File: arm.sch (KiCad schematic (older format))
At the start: 83 parts, among them J1 MICROSD_SOCKET_SPI, M1 MOTOR, P1 MicroUSB, P2 HC-05/06, P3 I²C_Port, P4 SPI_Port, P5 Ring_Port, Q1 MOSFET_N, Q2 IRLML2246TRPBF, Q3 IRLML2246TRPBF, Q4 MOSFET_P, Q5 IRLML2246TRPBF, Q6 IRLML2246TRPBF, Q7 IRLML2246TRPBF, Q8 IRLML2246TRPBF, Q9 IRLML2246TRPBF, SW1 SPST, SW2 SPST, U1 STM32F100C8, U2 LTC4054-4.2, U3 LTC2942-1, U4 HMC5883L, U5 MPU6050, U6 LTC3444, U7 BMP085, X1 8 mHz, X2 32.768(MS3V-T1R)

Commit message: Removed invisible labels
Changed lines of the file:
@@
 	1    0    0    -1
 $EndComp
-Text Label 900  4600 2    60   ~ 0
-VCC
-Text Label 900  4400 2    60   ~ 0
-SCL
 Text GLabel 4050 3450 0    60   BiDi ~ 0
 sda

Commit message: 6-pin ring port, RING_BTN2
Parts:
- removed P5: Ring_Port, symbol CONN_5
- added P?: CONN_6, symbol CONN_6
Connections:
- net GND: now also P?.6
- net accelgyro_interrupt: now also U1.39 (PB3/JTDO); no longer U1.45 (PB8/TIM4_CH3/TIM16_CH1/CEC)
- net at Q3.3 (D): now also P?.2
- net at Q5.1 (G), R14.1: now also P?.1
- net at Q6.3 (D): now also P?.3
- net at Q8.3 (D): now also P?.4
- net BT_LED1: no longer names the net of P2.31 (PIO8)
- net BT_LED1: no longer U1.39 (PB3/JTDO)
- net BT_LED2: no longer names the net of U1.40 (PB4/NJRST)
- net BT_LED2: no longer P2.32 (PIO9)
- net RING_BUTTON renamed RING_BTN1
- new net RING_BTN2: P?.5, U1.45 (PB8/TIM4_CH3/TIM16_CH1/CEC)

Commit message: Both PIO0 and PIO11 are connected to BT_KEY now. This is required for HM-10 and HC-05 compatibility.
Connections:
- net BT_KEY: now also P2.23 (PIO0)
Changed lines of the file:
@@
 Wire Wire Line
 	5700 6500 5700 6850
+Entry Wire Line
+	10800 2700 10900 2600
+Wire Wire Line
+	10350 2700 10800 2700
+Text Label 10400 2700 0    60   ~ 0
+BT_KEY
 $EndSCHEMATC

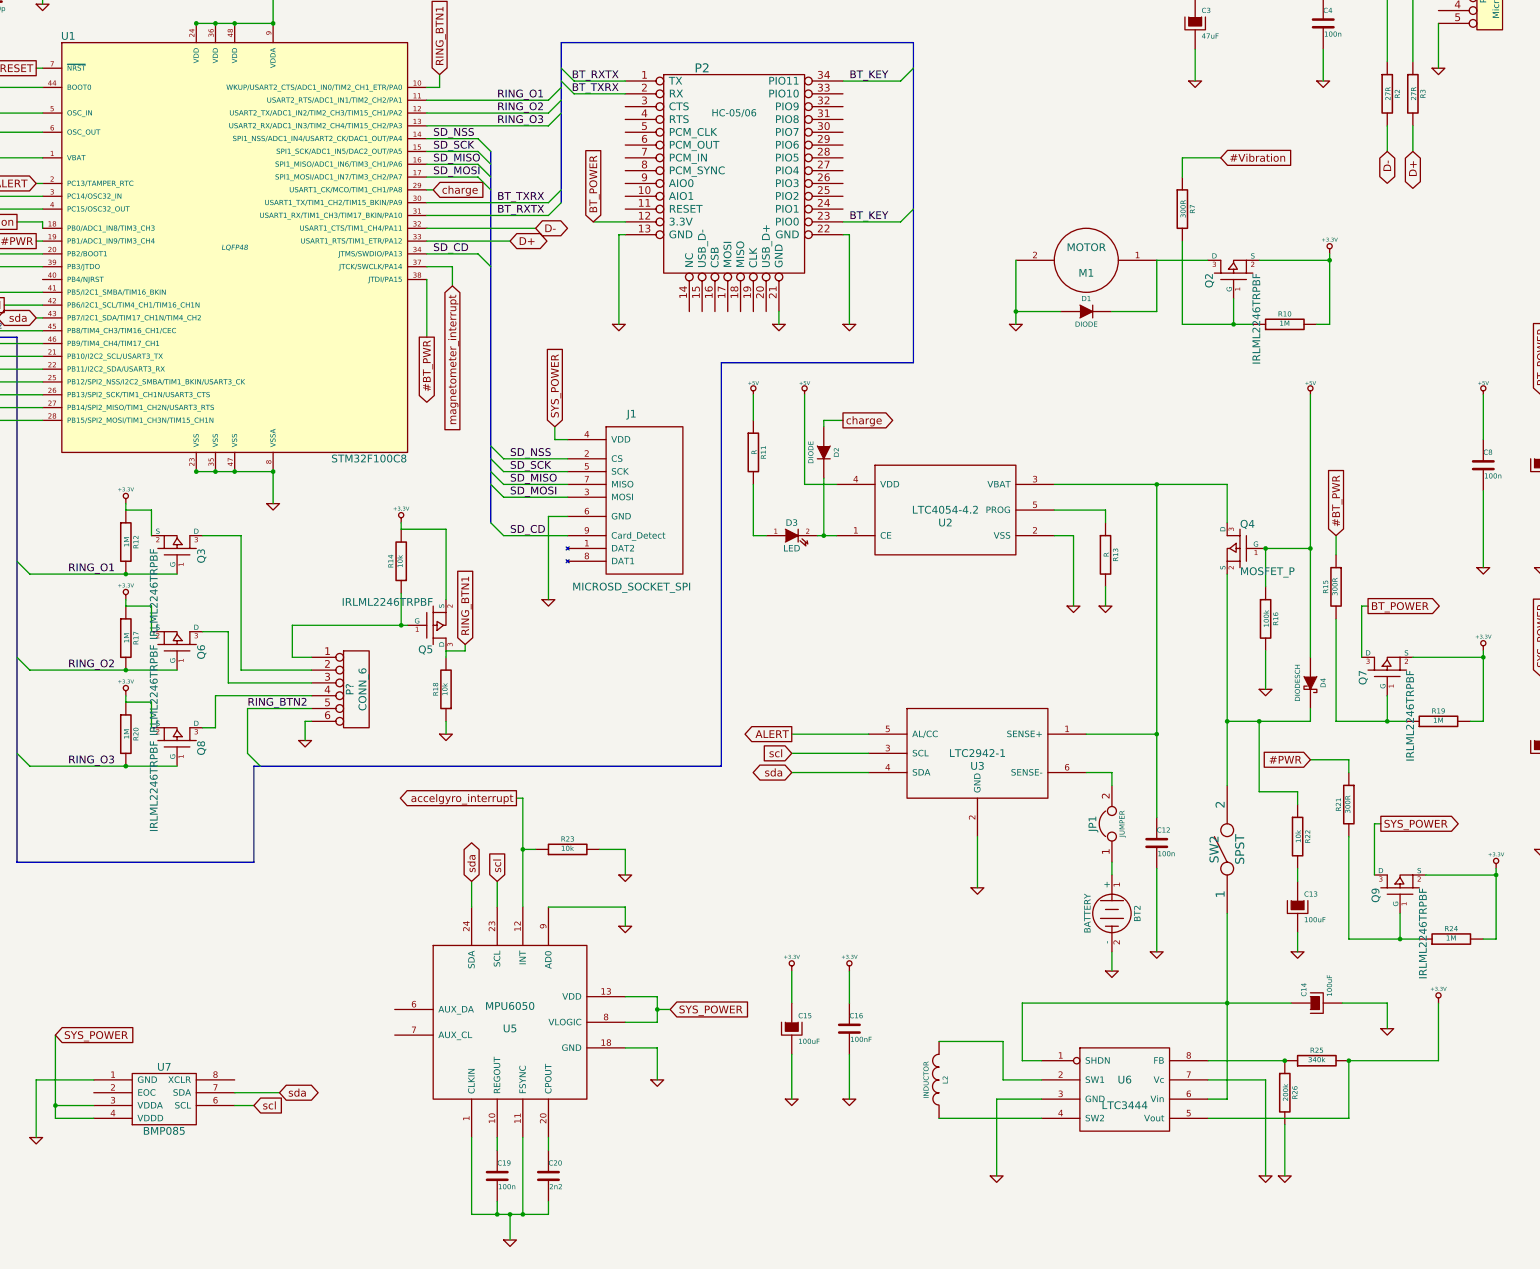
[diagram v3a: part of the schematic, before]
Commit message: Implemented an LTC3566-2 power management IC as primary power source / charge controller instead of previous problematic build.
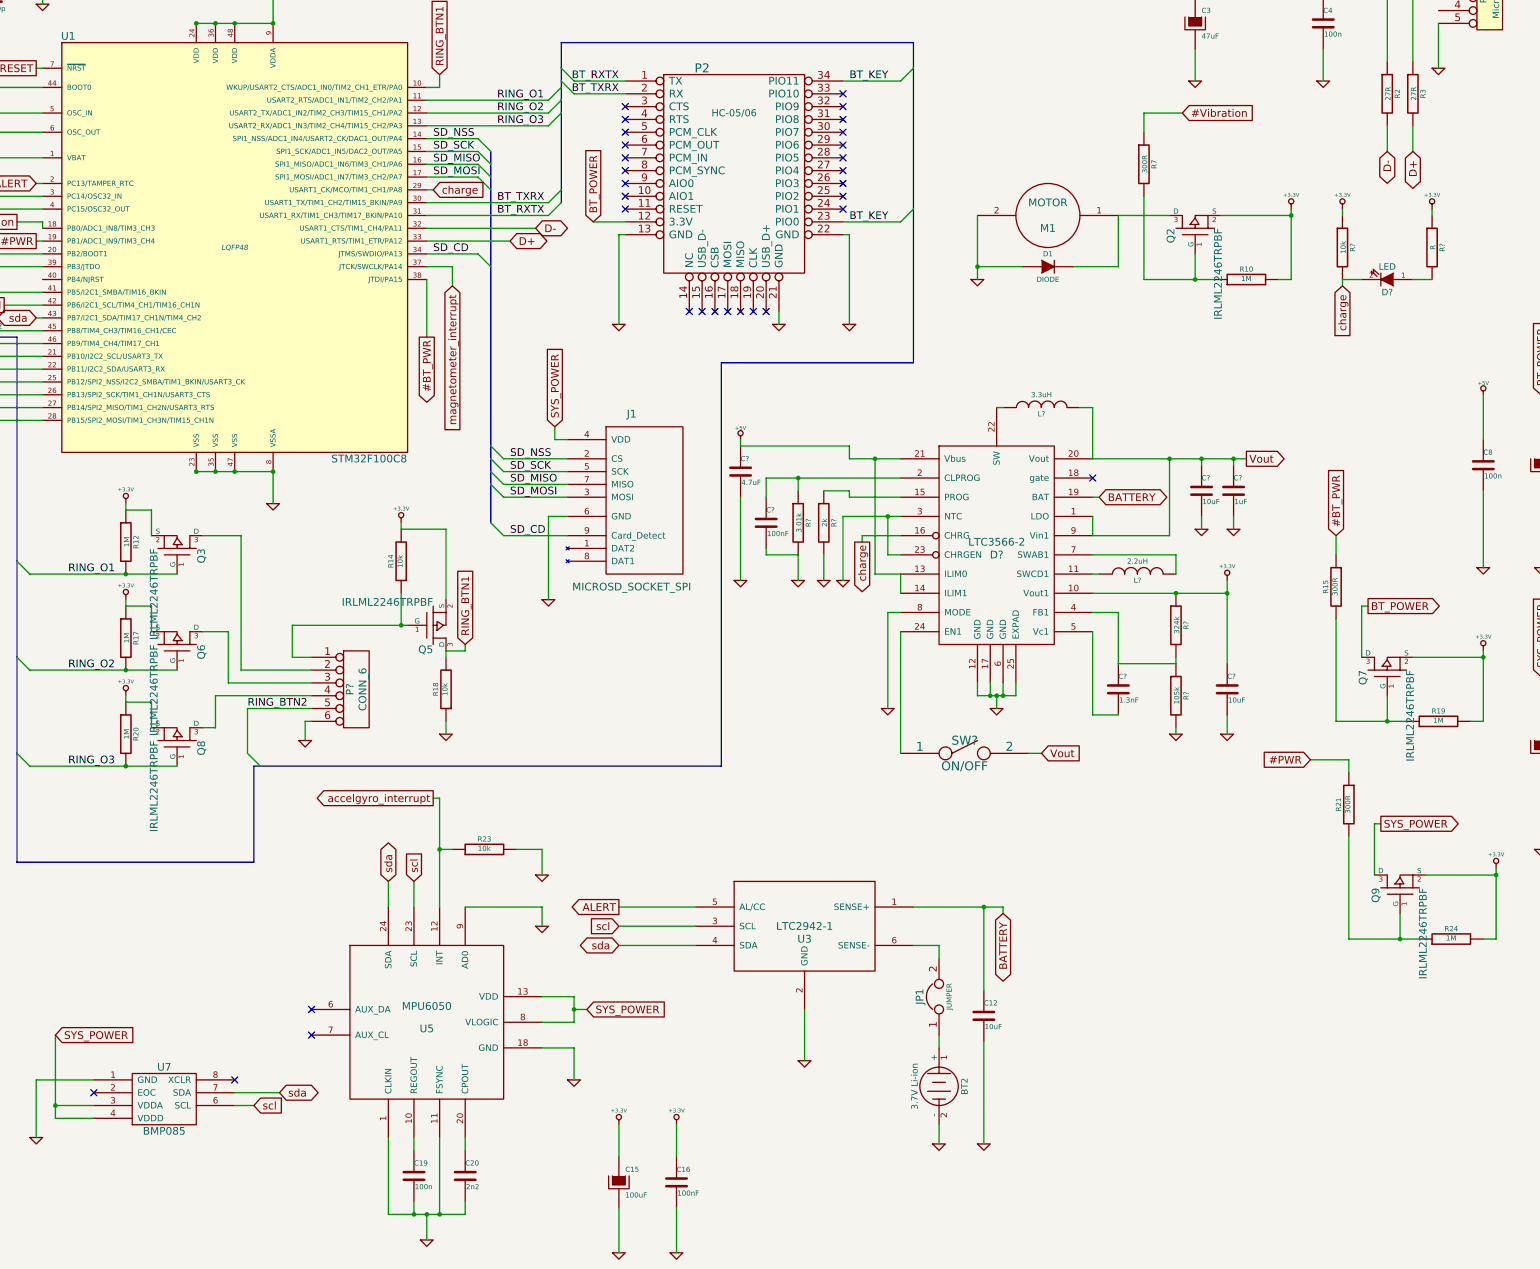
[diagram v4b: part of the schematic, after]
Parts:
- removed C13, C14: 100uF, ~, symbol CAPAPOL
- removed D2: DIODE, ~, symbol DIODE
- removed D3: LED, ~, symbol LED
- removed D4: DIODESCH, ~, symbol DIODESCH
- removed L2: INDUCTOR, ~, symbol INDUCTOR
- removed Q4: MOSFET_P, ~, symbol MOSFET_P
- removed R11, R13: R, ~, symbol R
- removed R16: 100k, ~, symbol R
- removed R22: 10k, ~, symbol R
- removed R25: 340k, ~, symbol R
- removed R26: 200k, ~, symbol R
- removed SW2: SPST, ~, symbol SPST
- removed U2: LTC4054-4.2, ~, symbol LTC4054-4.2
- removed U6: LTC3444, ~, symbol LTC3444
- added C?: 4.7uF, ~, symbol C
- added C?: 1.3nF, ~, symbol C
- added C? (x2): 10uF, ~, symbol C
- added C?: 1uF, ~, symbol C
- added C?: 100nF, ~, symbol C
- added D?: LTC3566-2, symbol LTC3566
- added D?: LED, ~, symbol LED
- added L?: 3.3uH, ~, symbol INDUCTOR
- added L?: 2.2uH, ~, symbol INDUCTOR
- added R?: 324k, ~, symbol R
- added R?: 105k, ~, symbol R
- added R?: 3.01k, ~, symbol R
- added R?: 2k, ~, symbol R
- added R?: 10k, ~, symbol R
- added R?: R, ~, symbol R
- added SW?: ON/OFF, ~, symbol SPST
- BT2: value BATTERY -> 3.7V Li-ion
- C12: value 100n -> 10uF
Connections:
- net +3.3V: now also C?.1, D?.10 (Vout1), R?.1, R?.1, R?.1
- net +5V: now also C?.1, D?.13 (ILIM0), D?.14 (ILIM1), D?.21 (Vbus)
- net GND: now also C?.2, C?.2, C?.2, C?.2, C?.2, D?.12 (GND), D?.17 (GND), D?.23 (CHRGEN), D?.25 (EXPAD), D?.3 (NTC), D?.6 (GND), D?.8 (MODE), R?.2, R?.2, R?.2
- net charge: now also D?.16 (CHRG), D?.2 (K), R?.2
- net BATTERY: now reaches C12.1, U3.1 (SENSE+)
- net BATTERY: now also D?.19 (BAT)
- new net: D?.11 (SWCD1), L?.1
- new net: D?.15 (PROG), R?.1
- new net: C?.1, D?.2 (CLPROG), R?.1
- new net: D?.22 (SW), L?.1
- new net: D?.24 (EN1), SW?.1
- new net: C?.1, D?.4 (FB1), R?.1, R?.2
- new net: C?.2, D?.5 (Vc1)
- new net: D?.7 (SWAB1), L?.2
- new net: D?.1 (A), R?.2
- new net Vout: C?.1, C?.1, D?.1 (LDO), D?.20 (Vout), D?.9 (Vin1), L?.2, SW?.2
- no-connect marks 0 -> 31
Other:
- moved on the sheet: BT2, C12, C15, C16, C19, C20, D1, JP1, M1, Q2, R10, R23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

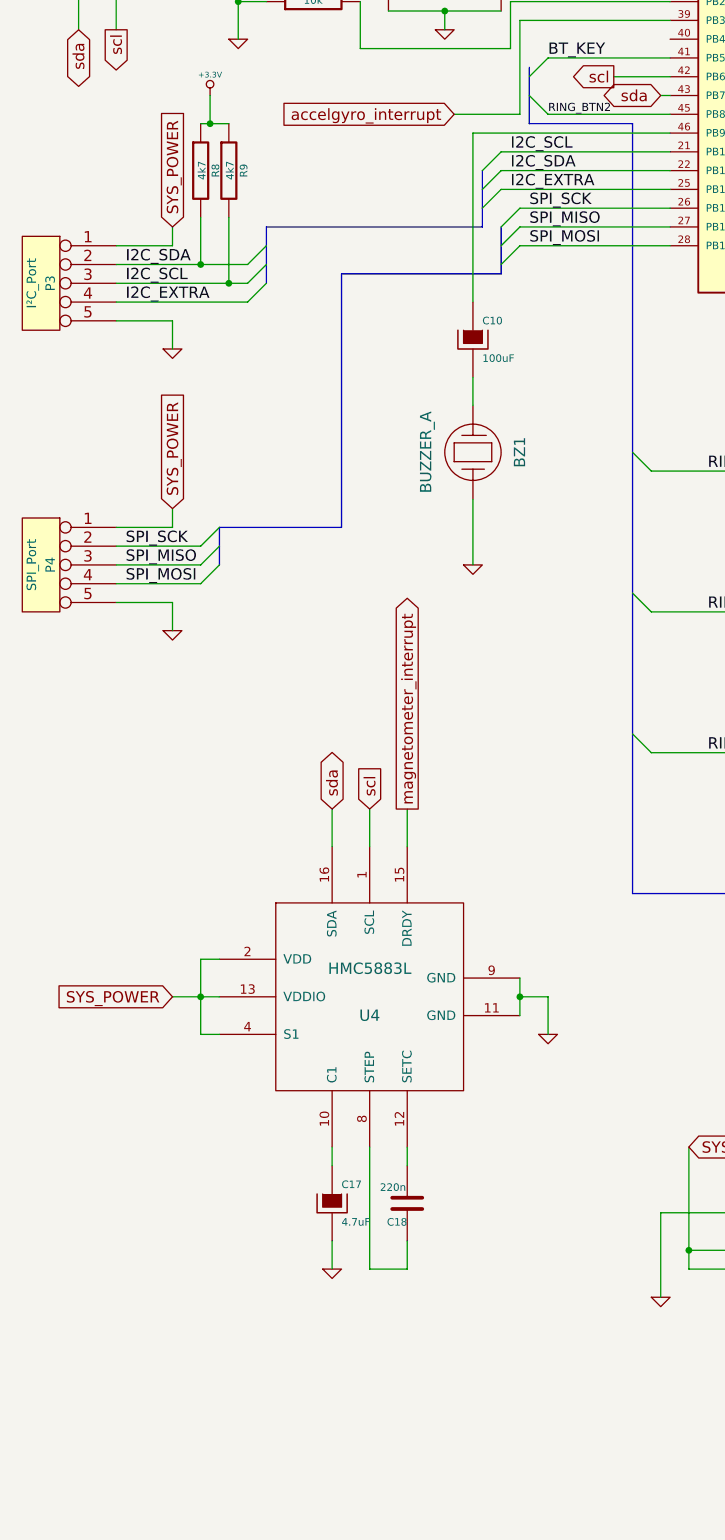
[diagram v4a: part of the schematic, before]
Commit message: added piezo buzzer instead of old one
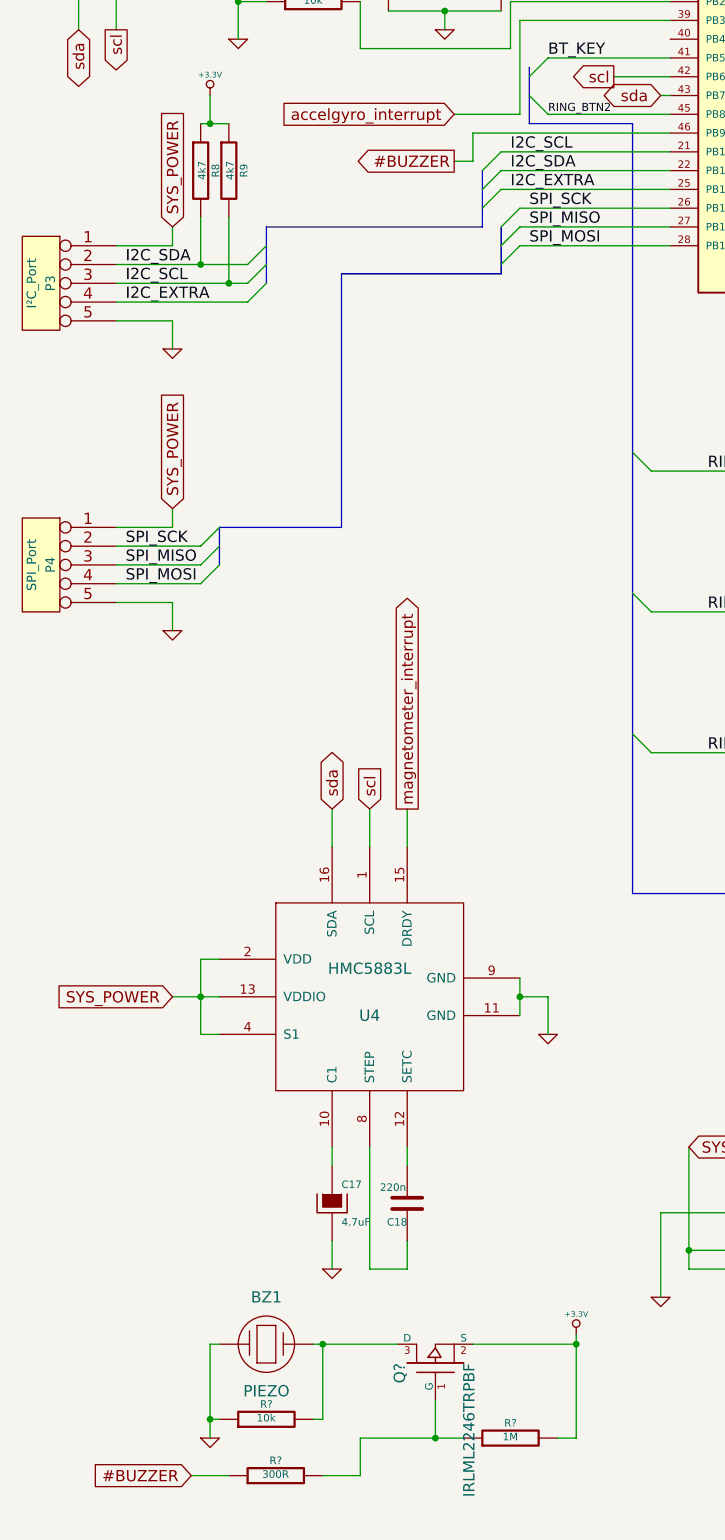
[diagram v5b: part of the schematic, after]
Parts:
- removed C10: 100uF, ~, symbol CAPAPOL
- added Q?: IRLML2246TRPBF, ~, symbol MOSFET_P
- added R?: 1M, ~, symbol R
- added R?: 300R, ~, symbol R
- added R?: 10k, ~, symbol R
- BZ1: value BUZZER_A -> PIEZO
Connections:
- net +3.3V: now also Q?.2 (S), R?.2
- net GND: now also BZ1.1, R?.1; no longer BZ1.2
- net #BUZZER: now reaches U1.46 (PB9/TIM4_CH4/TIM17_CH1)
- net #BUZZER: now also R?.1
- new net: BZ1.2, Q?.3 (D), R?.2
- new net: Q?.1 (G), R?.1, R?.2
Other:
- moved on the sheet: BZ1

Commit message: New super convenient push-button flashing system!
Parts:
- removed R6: 10k, ~, symbol R
- added C?: 100uF, ~, symbol CAPAPOL
- added FW/RST: SW_PUSH, ~, symbol SW_PUSH
- added Q?: IRLML2246TRPBF, ~, symbol MOSFET_P
- added R? (x2): 10k, ~, symbol R
- added R?: 500k, ~, symbol R
- SW1: value SPST -> BTN Function (FW/RST)
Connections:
- net +3.3V: now also SW1.2, R?.1; no longer SW1.1
- net GND: now also U1.20 (PB2/BOOT1), C?.2, FW/RST.2, R?.1
- net RESET: now also FW/RST.1, Q?.1 (G), R?.1, R?.2
- net FW/RST: now reaches Q1.1 (G), R1.2
- net FW/RST: now also SW1.1, Q?.2 (S), R?.2; no longer SW1.2, U1.44 (BOOT0)
- new net: C?.1, Q?.3 (D), R?.2, U1.44 (BOOT0)
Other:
- moved on the sheet: C5, C?, Q1, R1, R4, R5, SW1

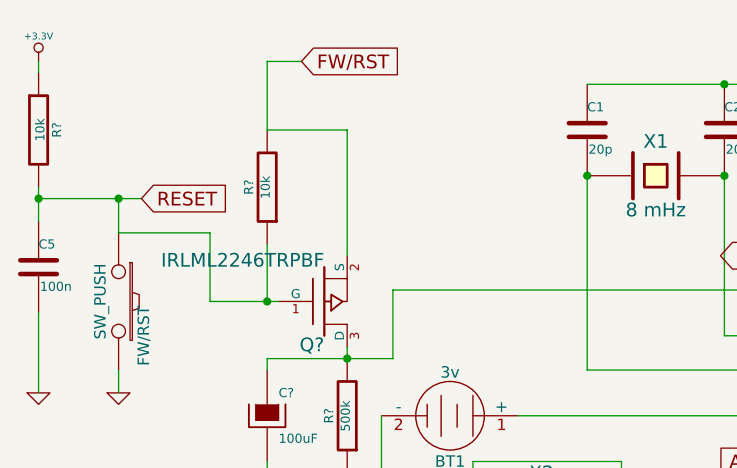
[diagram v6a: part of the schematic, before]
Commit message: removed unneeded resistor in flash-enable circuit
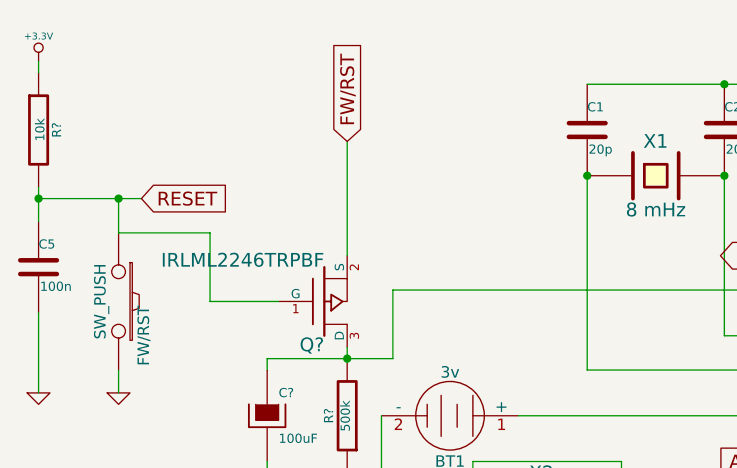
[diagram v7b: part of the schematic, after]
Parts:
- removed R?: 10k, ~, symbol R
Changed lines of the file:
@@
 Wire Wire Line
 	700  700  700  650
-Text GLabel 1850 650  2    60   Input ~ 0
+Text GLabel 2050 1000 1    60   Input ~ 0
 FW/RST
-$Comp
-L R R?
-U 1 1 53960BF8
-P 1700 1200
-F 0 "R?" V 1780 1200 40  0000 C CNN
-F 1 "10k" V 1707 1201 40  0000 C CNN
-F 2 "~" V 1630 1200 30  0000 C CNN
-F 3 "~" H 1700 1200 30  0000 C CNN
-	1    1700 1200
-	-1   0    0    1
-$EndComp
 $Comp
 L MOSFET_P Q?
@@
 $EndComp
 Wire Wire Line
-	1700 650  1700 950
-Wire Wire Line
-	1700 1450 1700 1700
-Wire Wire Line
-	1700 950  2050 950
-Wire Wire Line
-	2050 950  2050 1500
-Wire Wire Line
 	2050 1950 2050 1900
 Wire Wire Line
@@
 Wire Wire Line
 	1450 1400 1450 1700
-Connection ~ 1700 1700
-Wire Wire Line
-	1700 650  1850 650
 $Comp
 L CAPAPOL C?
@@
 Wire Wire Line
 	1700 2550 1700 2400
+Wire Wire Line
+	2050 1500 2050 1000
 $EndSCHEMATC

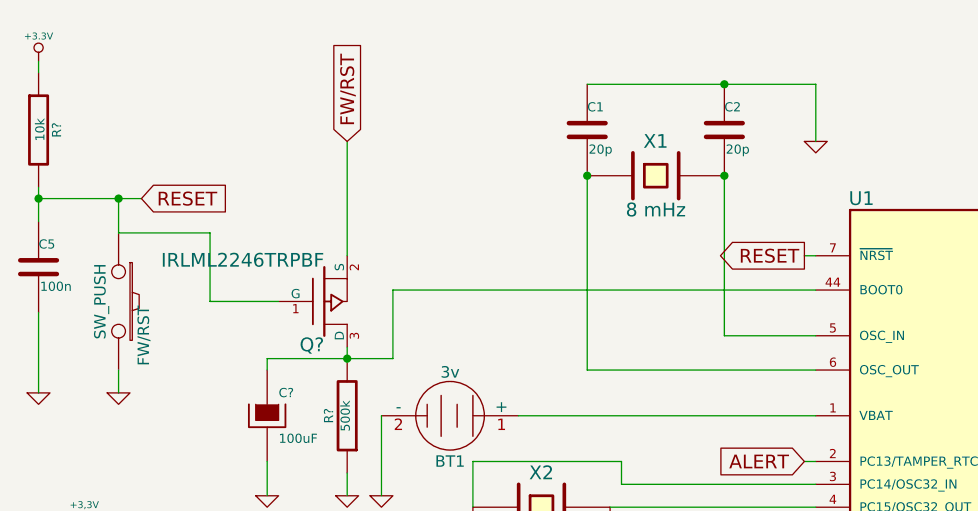
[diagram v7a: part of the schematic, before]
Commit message: Removed unnecessary RESET global label
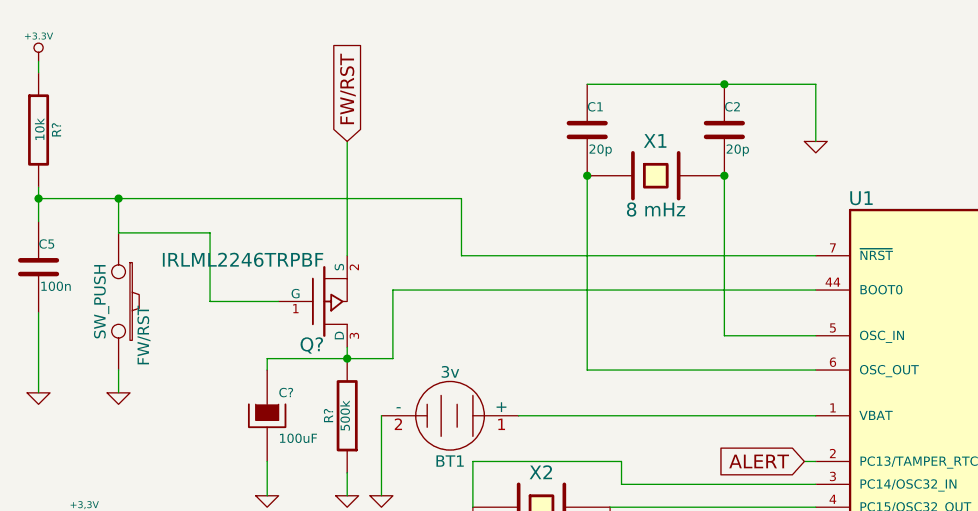
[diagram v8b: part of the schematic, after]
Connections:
- net RESET: no longer names the net of C5.1, FW/RST.1, Q?.1 (G), R?.2, U1.7 (~NRST)
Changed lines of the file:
@@
 Text GLabel 10500 5200 3    60   Output ~ 0
 charge
-Text GLabel 4050 1500 0    60   Output ~ 0
-RESET
 $Comp
 L C C5
@@
 	1    0    0    -1
 $EndComp
-Text GLabel 1150 1250 2    60   Input ~ 0
-RESET
 Text GLabel 7100 3600 3    60   Output ~ 0
 #BT_PWR
@@
 	7150 2450 7100 2450
 Wire Wire Line
-	700  1250 1150 1250
+	700  1250 2550 1250
 Wire Wire Line
 	7100 2950 7500 2950
@@
 	4750 4950 4750 4900
 Wire Wire Line
-	4050 1500 4100 1500
+	2550 1500 4100 1500
 Wire Wire Line
 	700  1750 700  2100
@@
 Wire Wire Line
 	2050 1500 2050 1000
+Wire Wire Line
+	2550 1250 2550 1500
 $EndSCHEMATC
